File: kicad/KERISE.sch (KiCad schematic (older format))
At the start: 4 parts, among them SW1 RESET, U1 ESP32-PICO-D4

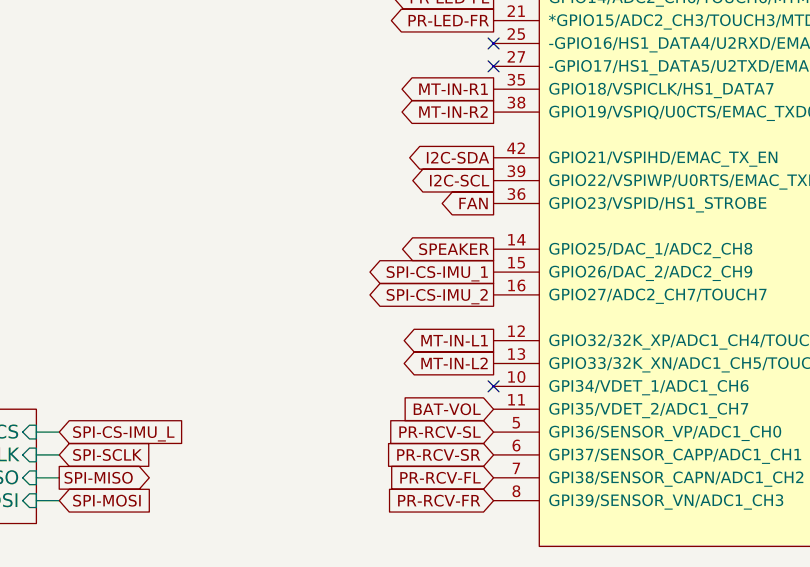
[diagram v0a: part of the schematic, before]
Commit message: 自動配線あと4本
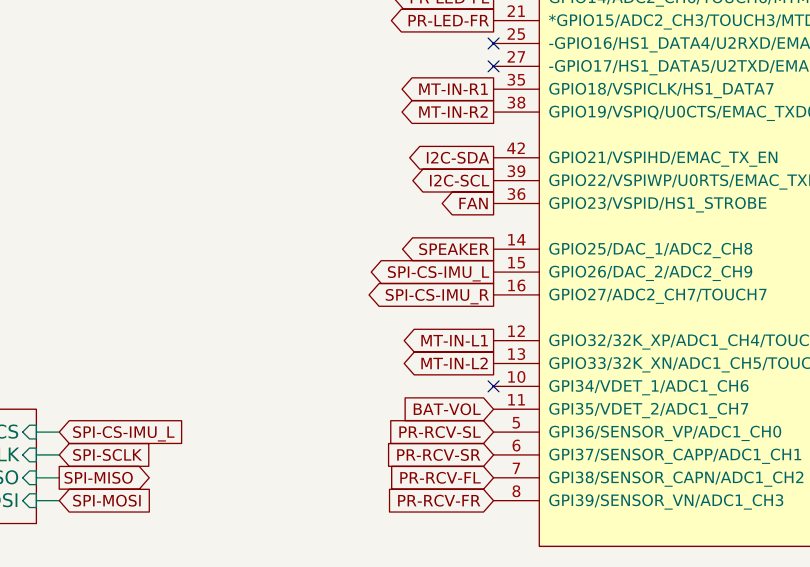
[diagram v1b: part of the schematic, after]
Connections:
- net SPI-CS-IMU_1 is gone; now on net SPI-CS-IMU_L: U1.15 (GPIO26/DAC_2/ADC2_CH9)
- net SPI-CS-IMU_2 is gone; now on net SPI-CS-IMU_R: U1.16 (GPIO27/ADC2_CH7/TOUCH7)
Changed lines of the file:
@@
 SPI-MOSI
 Text GLabel 5600 3800 0    50   Output ~ 0
-SPI-CS-IMU_1
+SPI-CS-IMU_L
 Text GLabel 5600 1600 0    50   Output ~ 0
 SPI-CS-ENC_L
@@
 SPI-MOSI
 Text GLabel 5600 3900 0    50   Output ~ 0
-SPI-CS-IMU_2
+SPI-CS-IMU_R
 NoConn ~ 9600 2600
 NoConn ~ 5600 1800

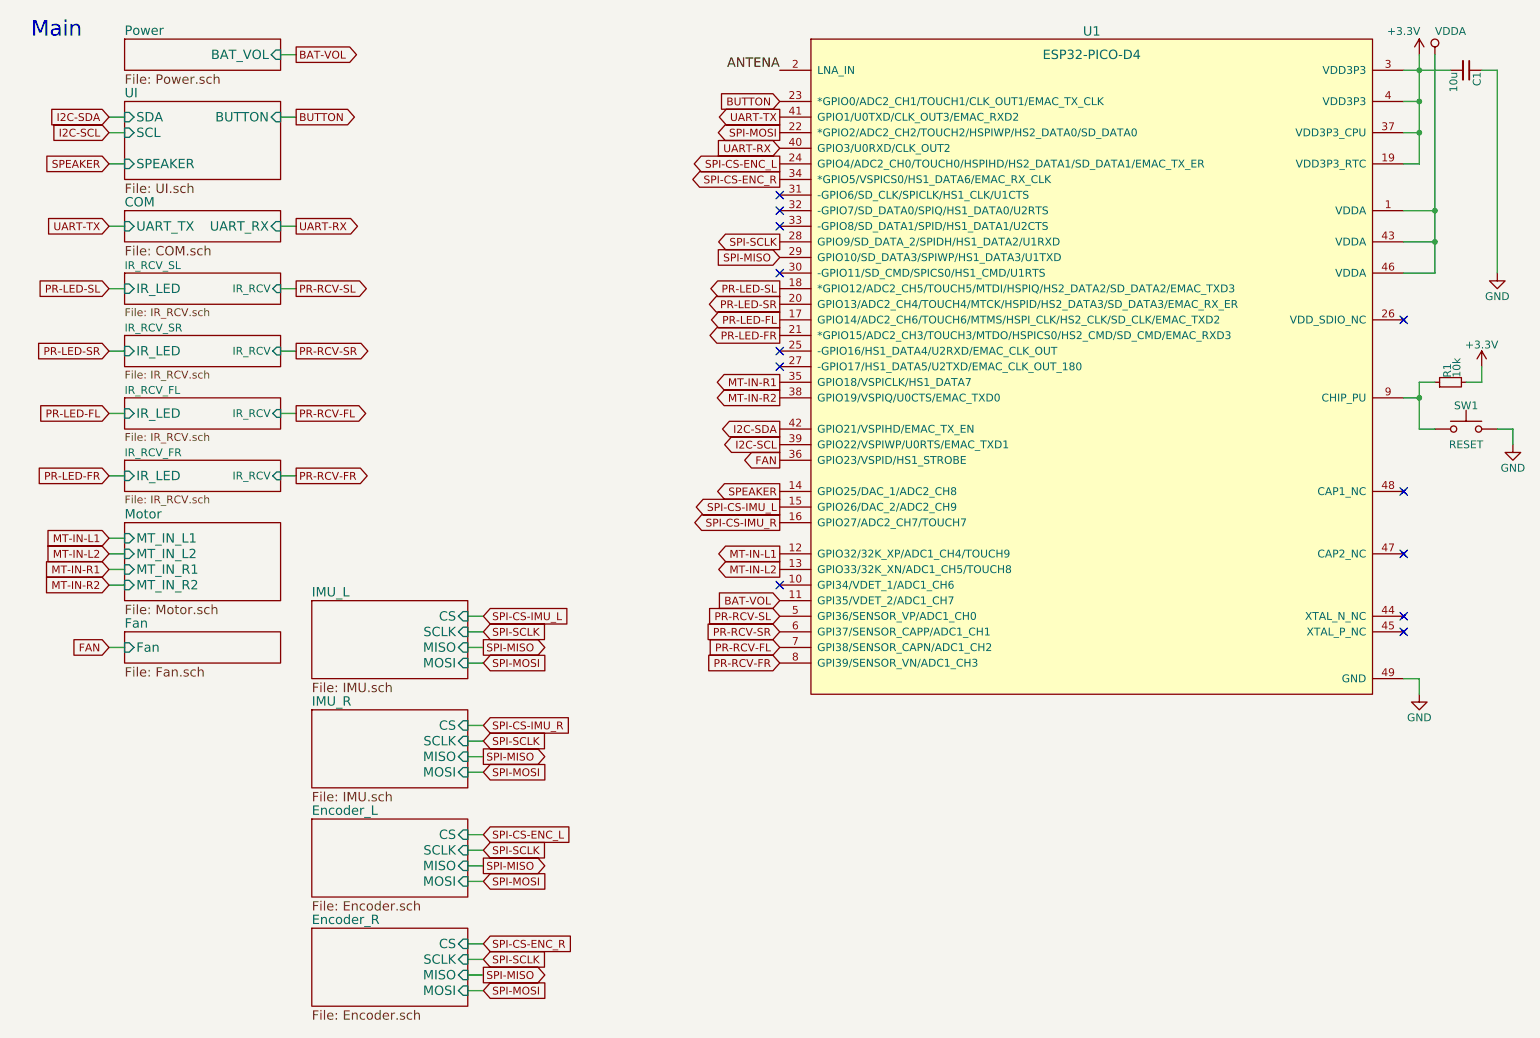
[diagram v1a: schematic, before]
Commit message: KERISEv4-5に向けて回路図を更新
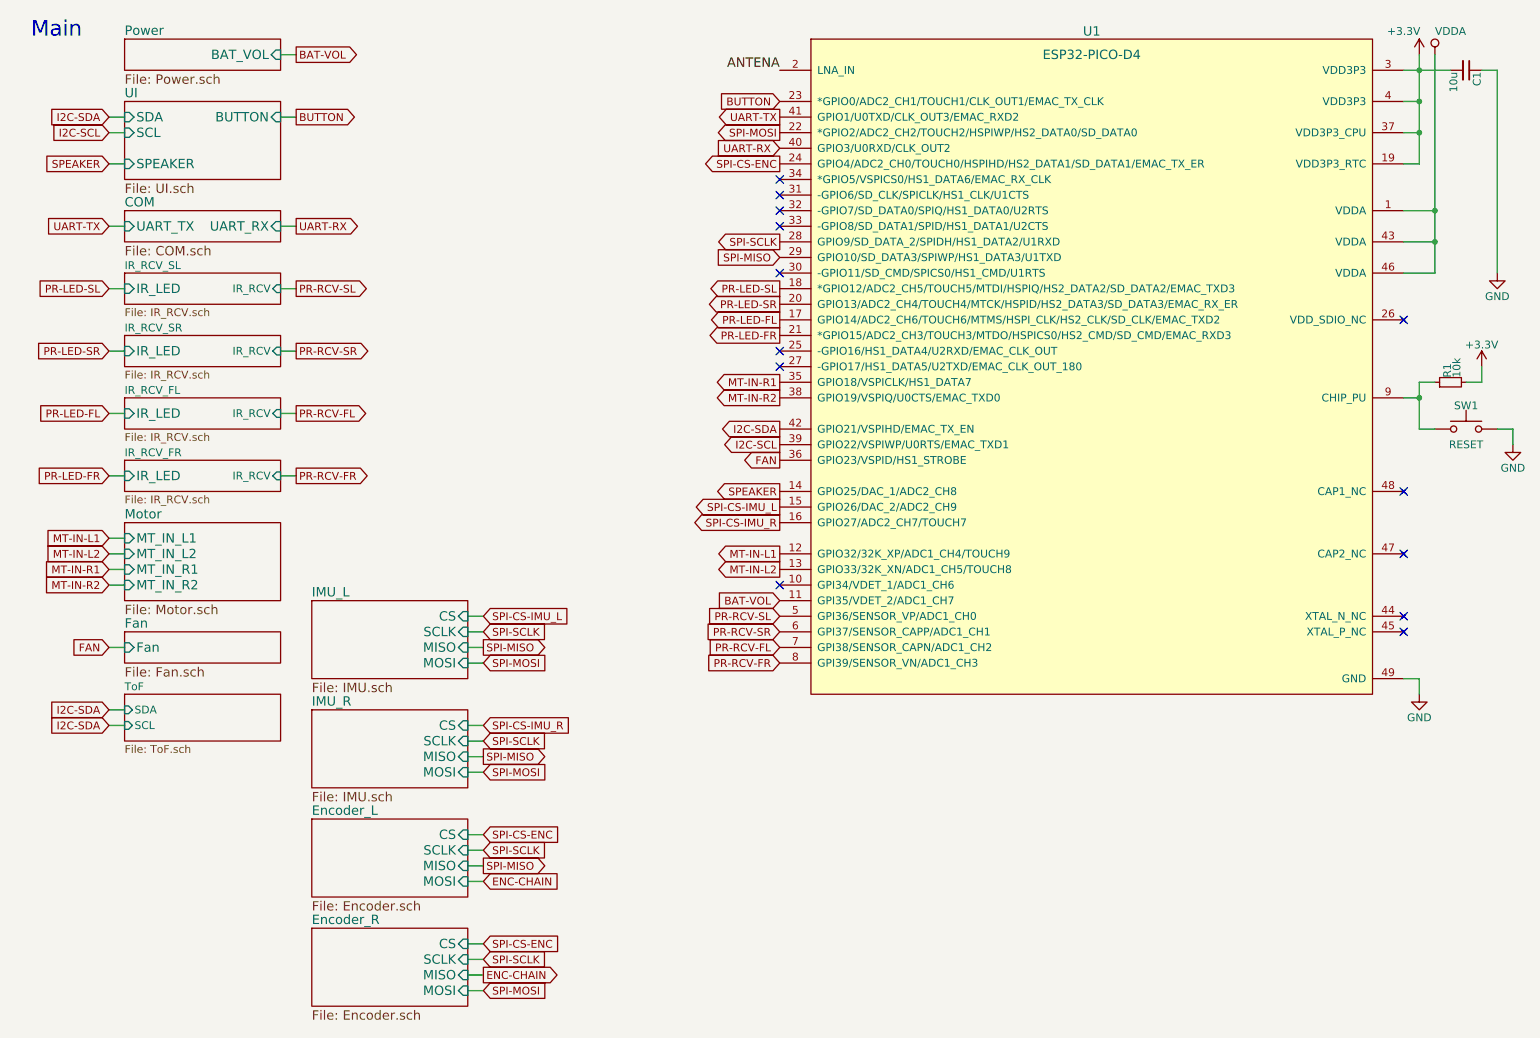
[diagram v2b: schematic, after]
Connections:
- net SPI-CS-ENC_L renamed SPI-CS-ENC
- net SPI-CS-ENC_R: no longer names the net of U1.34 (*GPIO5/VSPICS0/HS1_DATA6/EMAC_RX_CLK)
- no-connect marks 12 -> 13
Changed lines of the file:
@@
 $Descr A4 11693 8268
 encoding utf-8
-Sheet 1 14
+Sheet 1 15
 Title ""
 Date ""
@@
 SPI-MOSI
 Text GLabel 3700 5900 2    50   Input ~ 0
-SPI-CS-ENC_L
+SPI-CS-ENC
 Text GLabel 3700 6600 2    50   Input ~ 0
-SPI-CS-ENC_R
+SPI-CS-ENC
 Text GLabel 3700 6700 2    50   Input ~ 0
 SPI-SCLK
@@
 SPI-CS-IMU_L
 Text GLabel 5600 1600 0    50   Output ~ 0
-SPI-CS-ENC_L
+SPI-CS-ENC
 Text GLabel 5600 2100 0    50   Output ~ 0
 SPI-SCLK
@@
 	1    0    0    -1
 $EndComp
-Text GLabel 5600 1700 0    50   Output ~ 0
-SPI-CS-ENC_R
+Text GLabel 3700 6200 2    50   Input ~ 0
+ENC-CHAIN
+$Sheet
+S 1400 5000 1000 300
+U 5C29A0B1
+F0 "ToF" 50
+F1 "ToF.sch" 50
+F2 "SDA" I L 1400 5100 50
+F3 "SCL" I L 1400 5200 50
+$EndSheet
+Text GLabel 1300 5100 0    50   Input ~ 0
+I2C-SDA
+Text GLabel 1300 5200 0    50   Input ~ 0
+I2C-SDA
+Wire Wire Line
+	1300 5100 1400 5100
+Wire Wire Line
+	1400 5200 1300 5200
+NoConn ~ 5600 1700
 Text GLabel 3700 6800 2    50   Output ~ 0
-SPI-MISO
-Text GLabel 3700 6200 2    50   Input ~ 0
-SPI-MOSI
+ENC-CHAIN
 $EndSCHEMATC

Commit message: フットプリントを割り当て
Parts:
- C1: footprint Capacitors_SMD:C_0402_NoSilk -> Capacitor_SMD:C_0402_1005Metric
- R1: footprint Resistors_SMD:R_0201_NoSilk -> Resistor_SMD:R_0201_0603Metric
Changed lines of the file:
@@
 F 0 "R1" H 9930 3020 50  0000 L CNN
 F 1 "10k" H 9930 2960 50  0000 L CNN
-F 2 "Resistors_SMD:R_0201_NoSilk" H 9900 3000 50  0001 C CNN
+F 2 "Resistor_SMD:R_0201_0603Metric" H 9900 3000 50  0001 C CNN
 F 3 "" H 9900 3000 50  0000 C CNN
 	1    9900 3000
@@
 F 0 "C1" H 10010 1070 50  0000 L CNN
 F 1 "10u" H 10010 920 50  0000 L CNN
-F 2 "Capacitors_SMD:C_0402_NoSilk" H 10000 1000 50  0001 C CNN
+F 2 "Capacitor_SMD:C_0402_1005Metric" H 10000 1000 50  0001 C CNN
 F 3 "" H 10000 1000 50  0000 C CNN
 	1    10000 1000

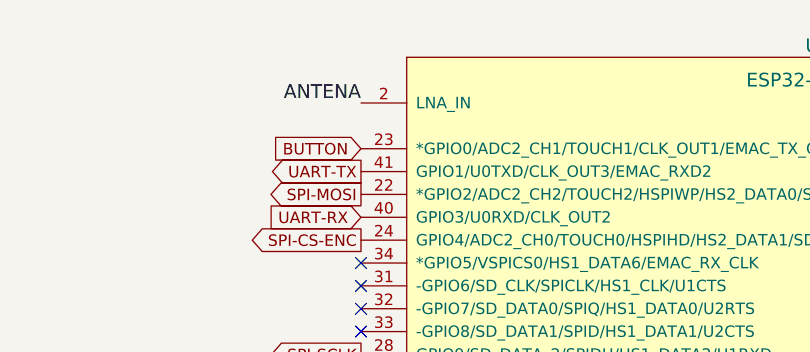
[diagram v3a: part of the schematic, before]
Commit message: アンテナを外側に配置
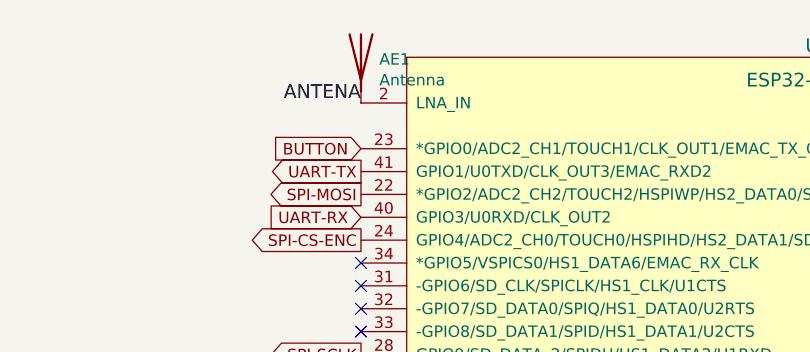
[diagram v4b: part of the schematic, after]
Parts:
- added AE1: Antenna, mouse:HIDDEN_PAD, symbol Device:Antenna
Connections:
- net ANTENA: now also AE1.1 (A)
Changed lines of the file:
@@
 Text GLabel 5600 3400 0    50   Output ~ 0
 I2C-SCL
-Text Label 5600 1000 2    60   ~ 0
-ANTENA
 $Comp
 L KERISE:ESP32-PICO-D4 U1
@@
 Text GLabel 3700 6800 2    50   Output ~ 0
 ENC-CHAIN
+$Comp
+L Device:Antenna AE1
+U 1 1 5C2F9122
+P 5600 800
+F 0 "AE1" H 5680 791 50  0000 L CNN
+F 1 "Antenna" H 5680 700 50  0000 L CNN
+F 2 "mouse:HIDDEN_PAD" H 5600 800 50  0001 C CNN
+F 3 "~" H 5600 800 50  0001 C CNN
+	1    5600 800
+	1    0    0    -1
+$EndComp
+Text Label 5600 1000 2    60   ~ 0
+ANTENA
 $EndSCHEMATC

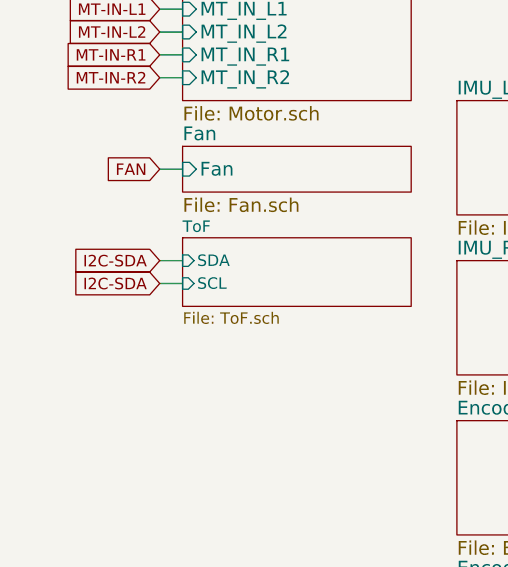
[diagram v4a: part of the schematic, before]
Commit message: LEDの抵抗を集合抵抗に変更
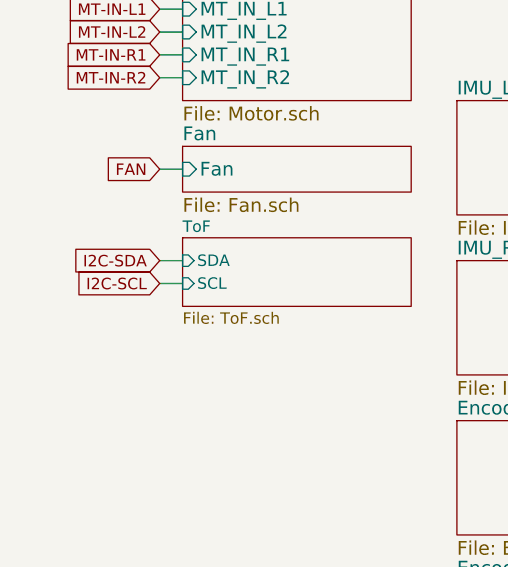
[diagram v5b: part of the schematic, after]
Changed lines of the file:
@@
 I2C-SDA
 Text GLabel 1300 5200 0    50   Input ~ 0
-I2C-SDA
+I2C-SCL
 Wire Wire Line
 	1300 5100 1400 5100
